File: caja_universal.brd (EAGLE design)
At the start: 100 x 80 mm, 34 parts, among them IC2 AD620N, IC3 TL084P, IC4 TL084P, IC5 LM317LD, IC6 LM318N

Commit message: Esquematico finalizado (v0), board en progreso
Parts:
- removed IC5: LM317LD, linear:SO08
- removed JP10, JP11, JP12: (no value), pinhead:1X01
- removed JP4, JP5, JP8, JP9: (no value), pinhead:1X02
- removed R12: (no value), resistor:0204/7
- added BNC-HALL, BNC-HR, BNC-PRESION, BNC-TENSION: (no value), pinhead:1X02
- added HALL-PLACA, HR-PLACA, TENSION-PLACA: (no value), pinhead:1X01
- added LM385-OFFSET: 2SC945, transistor:TO92-ECB
- added POT-GAIN, POT-OFFSET: (no value), pinhead:1X03
- added R-REG-FCORR: 10k, resistor:0204/7
- R-REG-OFFSET: value (none) -> 680k
- R10, R7, R8, R9: value (none) -> 10k
- R3, R4: value (none) -> 20k
- R5: value (none) -> 1k
- R6: value (none) -> 2k
- moved OPAMP-FCORR 110.8 mm to (30.5, 57.1), turned to 180 degrees
- moved PRESION-PLACA 105.2 mm to (77.5, 72.4)
- moved CHECK 103.8 mm to (55.9, 72.4)
- moved CORRIENTE-PLACA 95.6 mm to (40.6, 72.4), turned to 180 degrees
- moved RCHECK 85.2 mm to (57.1, 63.5), turned to 270 degrees
- moved ALIMENTACION-PLACA 80.7 mm to (17.8, 63.5)
- moved CHECK-LED 80.1 mm to (55.9, 54.6), turned to 180 degrees
- moved ALIMENTACION-BATERIAS 71.1 mm to (20.3, 74.9)
- moved LM385-FCORR 60.5 mm to (11.4, 50.8), turned to 270 degrees
- moved SWITCH 60.2 mm to (19.1, 68.6)
- renumbered IC2 to PREAMP-PRESION, IC6 to SEGUIDOS-PREAMP-PRESION, R2 to R-REG-OFFSET
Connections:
- new net -1.25V: IC3.8, IC3.9, POT-OFFSET.3
- new net 1.25V: IC3.1, IC3.2, POT-OFFSET.2, R3.1
- new net HALL: BNC-HALL.1, HALL-PLACA.1
- new net HR: BNC-HR.1, HR-PLACA.1
- new net N$10: IC3.13, R5.2, R6.1
- new net N$11: IC3.14, IC4.3, R6.2
- new net N$12: IC4.6, R10.2, R7.1, R9.2
- new net N$13: R9.1, SEGUIDOS-PREAMP-PRESION.2, SEGUIDOS-PREAMP-PRESION.6
- new net N$14: IC4.10, IC4.7, R7.2
- new net N$15: IC4.8, IC4.9, R8.1
- new net N$16: IC4.13, POT-GAIN.3, R8.2
- new net N$6: IC3.6, R3.2, R4.1
- new net N$7: IC3.3, LM385-OFFSET.C, R-REG-OFFSET.2
- new net N$8: IC3.10, IC3.7, R4.2
- new net N$9: IC4.1, IC4.2, R10.1
- new net OFFSET: IC3.12, POT-OFFSET.1
- new net PRESION: BNC-PRESION.1, IC4.14, POT-GAIN.2
- new net TENSION: BNC-TENSION.1, TENSION-PLACA.1
- net +12V: now also R-REG-FCORR.2, R-REG-OFFSET.1, SEGUIDOS-PREAMP-PRESION.7
- net -12V: now also SEGUIDOS-PREAMP-PRESION.4
- net 0V: now also BNC-HALL.2, BNC-HR.2, BNC-PRESION.2, BNC-TENSION.2, IC3.5, IC4.5, LM385-OFFSET.B, LM385-OFFSET.E, R5.1
- net N$3: now also R-REG-FCORR.1
- net PRESION-PREAMP: now also SEGUIDOS-PREAMP-PRESION.3
- net V+: no longer SEGUIDOS-PREAMP-PRESION.7
- net V-: no longer SEGUIDOS-PREAMP-PRESION.4
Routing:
- net +12V: track 0.00 -> 45.3 mm
- net -12V: track 0.00 -> 14.0 mm
- net N$3: track 0.00 -> 10.2 mm
- net -12VBAT: track 0.00 -> 6.35 mm
- net +12VBAT: track 0.00 -> 6.35 mm
- net N$2: track 0.00 -> 5.08 mm
- net N$1: track 0.00 -> 5.08 mm
- added copper zone on layer 1, net 0V

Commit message: Avanzando...
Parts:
- moved LM385-OFFSET 154.7 mm to (67.3, 40.6), turned to 270 degrees
- moved R3 122.1 mm to (66.0, 10.2)
- moved SEGUIDOS-PREAMP-PRESION 114.8 mm to (36.8, 34.3), turned to 180 degrees
- moved R4 102.4 mm to (76.2, 10.2)
- moved R6 99.2 mm to (58.4, 27.9), turned to 180 degrees
- moved R10 92.0 mm to (48.3, 22.9), turned to 180 degrees
- moved IC3 91.1 mm to (67.3, 19.1)
- moved R-REG-OFFSET 90.9 mm to (49.5, 34.3), turned to 90 degrees
- moved R5 88.4 mm to (58.4, 31.8)
- moved R7 88.4 mm to (35.6, 22.9), turned to 180 degrees
- moved IC4 88.1 mm to (44.5, 15.2), turned to 180 degrees
- moved RG-PRESION 78.9 mm to (27.9, 34.3), turned to 90 degrees
- moved R8 77.8 mm to (43.2, 6.35)
- moved R-FCORR 74.3 mm to (39.4, 71.1), turned to 180 degrees
- moved R9 69.9 mm to (35.6, 25.4)
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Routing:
- net +12V: track 45.3 -> 104.1 mm
- net -12V: track 14.0 -> 52.1 mm
- net PRESION: track 0.00 -> 35.6 mm
- net N$16: track 0.00 -> 25.4 mm
- net N$11: track 0.00 -> 24.1 mm
- net N$8: track 0.00 -> 22.9 mm
- net N$7: track 0.00 -> 20.3 mm
- net N$13: track 0.00 -> 19.1 mm
- net TENSION: track 0.00 -> 15.2 mm
- net N$12: track 0.00 -> 14.0 mm
- net HR: track 0.00 -> 14.0 mm
- net 1.25V: track 0.00 -> 14.0 mm
- net N$10: track 0.00 -> 8.89 mm
- net N$6: track 0.00 -> 7.62 mm
- net N$15: track 0.00 -> 7.62 mm
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
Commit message: Terminada primera version de la placa
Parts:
- removed ALIMENTACION-BATERIAS, ALIMENTACION-PLACA: (no value), pinhead:1X03
- removed CORRIENTE-PLACA, PRESION-PLACA: (no value), pinhead:1X02
- removed LM385-FCORR, LM385-OFFSET: 2SC945, transistor:TO92-ECB
- removed OPAMP-FCORR, SEGUIDOS-PREAMP-PRESION: LM318N, linear:DIL08
- removed PREAMP-PRESION: AD620N, analog-devices:DIL08
- removed R-FCORR, RG-PRESION: 820, resistor:0204/7
- removed R-REG-FCORR: 10k, resistor:0204/7
- removed R-REG-OFFSET: 680k, resistor:0204/7
- removed SWITCH: (no value), pinhead:1X04
- removed TENSION-PLACA: (no value), pinhead:1X01
- added +12V-FUSE, -12V-FUSE, I-PLACA, P-PLACA, T-PLACA: (no value), pinhead:1X02
- added D1, D2: LM385, lm385:TO-92
- added IC1, IC5: NE5534AN, linear:DIL08
- added IC2: AD620N, analog-devices:DIL08
- added R1, R2: 820, resistor:0204/7
- added R11: 10k, resistor:0204/7
- added R12: 680k, resistor:0204/7
- added SWITCH-GRAL, SWITCH-P: (no value), pinhead:1X04
- added V-BAT, V-PLACA: (no value), pinhead:1X03
- BNC-HALL, BNC-HR, BNC-PRESION, BNC-TENSION: value (none) -> A1944-50; device pinhead:1X02 -> con-coax:A1944
- HALL-PLACA, HR-PLACA: device pinhead:1X01 -> pinhead:1X02
- moved BNC-TENSION 69.5 mm to (36.2, 7.79), turned to 0 degrees
- moved POT-OFFSET 65.4 mm to (4.73, 35.0), turned to 270 degrees
- moved BNC-HALL 55.1 mm to (94.5, 7.79), turned to 0 degrees
- moved BNC-HR 52.4 mm to (63.8, 8.00), turned to 0 degrees
- moved BNC-PRESION 45.9 mm to (7.53, 7.49)
- moved R4 37.7 mm to (50.7, 37.9), turned to 180 degrees
- moved POT-GAIN 30.6 mm to (4.77, 25.1), turned to 90 degrees
- moved R10 27.0 mm to (23.7, 33.9)
- moved HALL-PLACA 25.7 mm to (56.4, 60.6)
- moved HR-PLACA 25.2 mm to (67.1, 60.5), turned to 180 degrees
- moved R3 24.7 mm to (58.4, 33.6), turned to 180 degrees
- moved R8 22.8 mm to (23.2, 17.3)
- moved IC4 22.7 mm to (23.9, 24.8)
- moved R9 22.6 mm to (20.0, 41.9)
- moved R7 21.9 mm to (19.6, 37.9)
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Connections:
- net PRESION renamed POUT
- removed net 0VBAT: ALIMENTACION-BATERIAS.2
- removed net PRESION-PREAMP: PREAMP-PRESION.6, SEGUIDOS-PREAMP-PRESION.3
- new net +12V-PRESION: CHECK.1, IC1.7, IC2.7, IC5.7, R11.2, R12.1, SWITCH-P.2
- new net +12VFUSE: +12V-FUSE.1, SWITCH-GRAL.1
- new net -12V-PRESION: IC1.4, IC2.4, IC5.4, SWITCH-P.4
- new net -12VFUSE: -12V-FUSE.1, SWITCH-GRAL.3
- new net P-PREAMP: IC2.6, IC5.3
- net +12V: now also +12V-FUSE.2, SWITCH-P.1, V-PLACA.1; no longer ALIMENTACION-PLACA.1, CHECK.1, OPAMP-FCORR.7, PREAMP-PRESION.7, R-REG-FCORR.2, R-REG-OFFSET.1, SEGUIDOS-PREAMP-PRESION.7, SWITCH.1
- net +12VBAT: now also SWITCH-GRAL.2, V-BAT.1; no longer ALIMENTACION-BATERIAS.1, SWITCH.2
- net +I: now also I-PLACA.1, IC1.6; no longer CORRIENTE-PLACA.1, OPAMP-FCORR.6
- net -12V: now also -12V-FUSE.2, SWITCH-P.3, V-PLACA.3; no longer ALIMENTACION-PLACA.3, OPAMP-FCORR.4, PREAMP-PRESION.4, SEGUIDOS-PREAMP-PRESION.4, SWITCH.3
- net -12VBAT: now also SWITCH-GRAL.4, V-BAT.3; no longer ALIMENTACION-BATERIAS.3, SWITCH.4
- net -I: now also I-PLACA.2, IC1.2, R2.2; no longer CORRIENTE-PLACA.2, OPAMP-FCORR.2, R-FCORR.2
- net 0V: now also BNC-HALL.3, BNC-HALL.4, BNC-HALL.5, BNC-HR.3, BNC-HR.4, BNC-HR.5, BNC-PRESION.3, BNC-PRESION.4, BNC-PRESION.5, BNC-TENSION.3, BNC-TENSION.4, BNC-TENSION.5, D1.-, D1.FB, D2.-, D2.FB, IC2.5, R2.1, V-BAT.2, V-PLACA.2; no longer ALIMENTACION-PLACA.2, LM385-FCORR.B, LM385-FCORR.E, LM385-OFFSET.B, LM385-OFFSET.E, PREAMP-PRESION.5, R-FCORR.1
- net HALL: now also HALL-PLACA.2; no longer HALL-PLACA.1
- net HR: now also HR-PLACA.2; no longer HR-PLACA.1
- net N$13: now also IC5.2, IC5.6; no longer SEGUIDOS-PREAMP-PRESION.2, SEGUIDOS-PREAMP-PRESION.6
- net N$3: now also D2.+, IC1.3, R11.1; no longer LM385-FCORR.C, OPAMP-FCORR.3, R-REG-FCORR.1
- net N$4: now also IC2.1, R1.2; no longer PREAMP-PRESION.1, RG-PRESION.2
- net N$5: now also IC2.8, R1.1; no longer PREAMP-PRESION.8, RG-PRESION.1
- net N$7: now also D1.+, R12.2; no longer LM385-OFFSET.C, R-REG-OFFSET.2
- net P+: now also IC2.3, P-PLACA.1; no longer PREAMP-PRESION.3, PRESION-PLACA.1
- net P-: now also IC2.2, P-PLACA.2; no longer PREAMP-PRESION.2, PRESION-PLACA.2
- net TENSION: now also T-PLACA.2; no longer TENSION-PLACA.1
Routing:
- net +12V-PRESION: track 0.00 -> 163.9 mm
- net V-: track 0.00 -> 146.7 mm
- net N$7: track 20.3 -> 134.4 mm
- net +12V: track 104.1 -> 203.0 mm
- net OFFSET: track 0.00 -> 89.6 mm
- net TENSION: track 15.2 -> 104.8 mm
- net HALL: track 6.35 -> 85.6 mm
- net HR: track 14.0 -> 85.0 mm
- net -12V: track 52.1 -> 119.9 mm
- net 1.25V: track 14.0 -> 81.7 mm
- net -1.25V: track 0.00 -> 62.8 mm
- net -12V-PRESION: track 0.00 -> 61.4 mm
- net V+: track 0.00 -> 55.4 mm
- net +I: track 0.00 -> 31.9 mm
- net P-PREAMP: track 0.00 -> 26.8 mm
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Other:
- board size 100 x 80 mm -> 117.8 x 66.5 mm

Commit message: Version para revisar (JyG)
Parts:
- IC1, IC5: value NE5534AN -> AD711N; device linear:DIL08 -> analog-devices:DIL08
- moved V-PLACA 50.2 mm to (61.0, 80.9)
- moved HALL-PLACA 42.9 mm to (94.4, 80.6)
- moved -12V-FUSE 32.4 mm to (83.8, 67.9), turned to 90 degrees
- moved D1 28.2 mm to (65.7, 44.4), turned to 270 degrees
- moved HR-PLACA 26.2 mm to (84.1, 80.5)
- moved +12V-FUSE 25.0 mm to (79.2, 67.7), turned to 90 degrees
- moved I-PLACA 21.9 mm to (31.6, 80.7)
- moved SWITCH-P 21.5 mm to (19.8, 80.7)
- moved D2 20.6 mm to (57.7, 56.3), turned to 180 degrees
- moved CHECK 20.6 mm to (44.0, 80.6)
- moved P-PLACA 20.1 mm to (2.33, 80.4)
- moved T-PLACA 20.1 mm to (73.0, 80.6)
- moved IC1 19.6 mm to (59.0, 67.0)
- moved RCHECK 18.8 mm to (70.8, 68.0)
- moved POT-GAIN 17.4 mm to (0.23, 41.9), turned to 270 degrees
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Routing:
- net +12V: track 203.0 -> 65.3 mm
- net V-: track 146.7 -> 34.8 mm
- net N$7: track 134.4 -> 35.3 mm
- net +12V-PRESION: track 163.9 -> 116.3 mm, vias 0 -> 1
- net -12V: track 119.9 -> 82.3 mm
- net POUT: track 50.0 -> 81.6 mm
- net -I: track 19.2 -> 43.8 mm
- net N$13: track 37.1 -> 17.3 mm
- net V+: track 55.4 -> 36.1 mm
- net +12VBAT: track 26.4 -> 9.82 mm
- net -12VBAT: track 24.4 -> 9.94 mm
- net -12V-PRESION: track 61.4 -> 75.6 mm
- net N$16: track 33.1 -> 47.2 mm
- net N$2: track 15.4 -> 29.1 mm
- net OFFSET: track 89.6 -> 76.9 mm
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- added copper zone on layer 16, net 0V
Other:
- board size 117.8 x 66.5 mm -> 137.8 x 101.5 mm
- board text added: "LSD - Tecnologia Hibrida de Cajas"

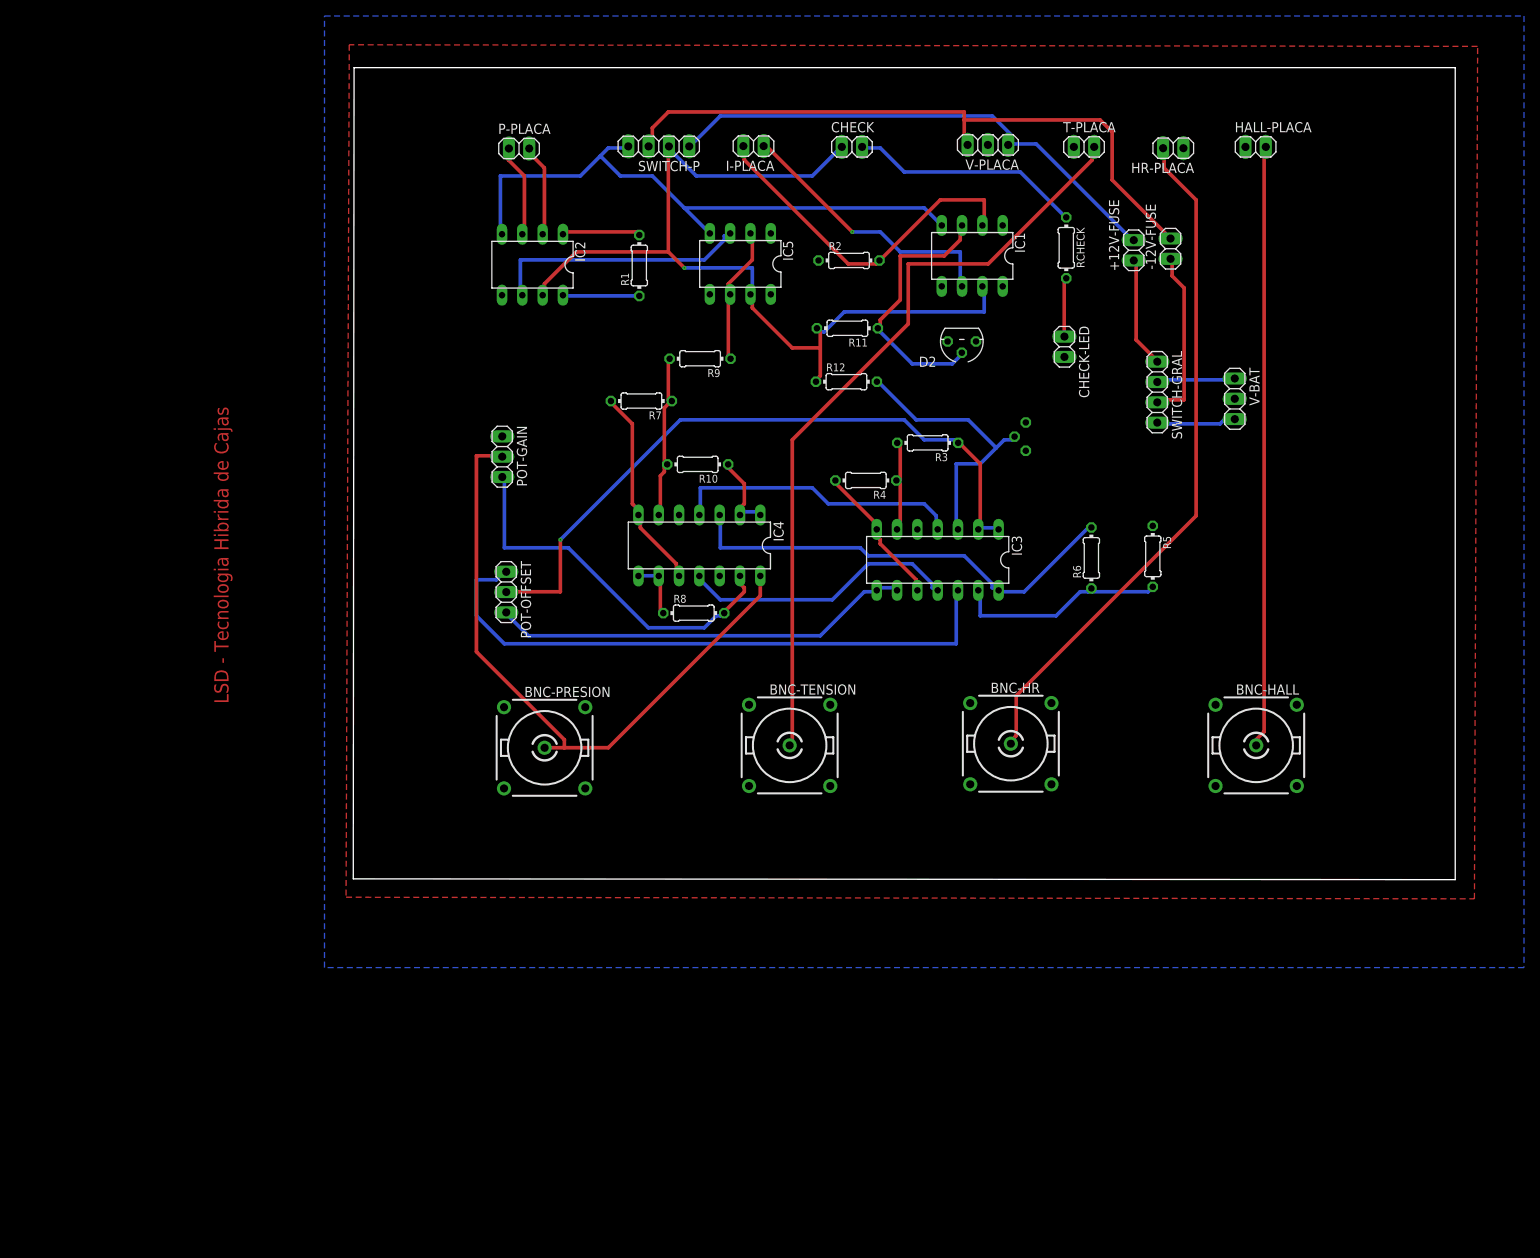
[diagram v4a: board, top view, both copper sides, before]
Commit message: Agregamos con Juan uno GND que faltaban. Falta ver alimentacion de TL084 y cambiar valor resistencia del LED
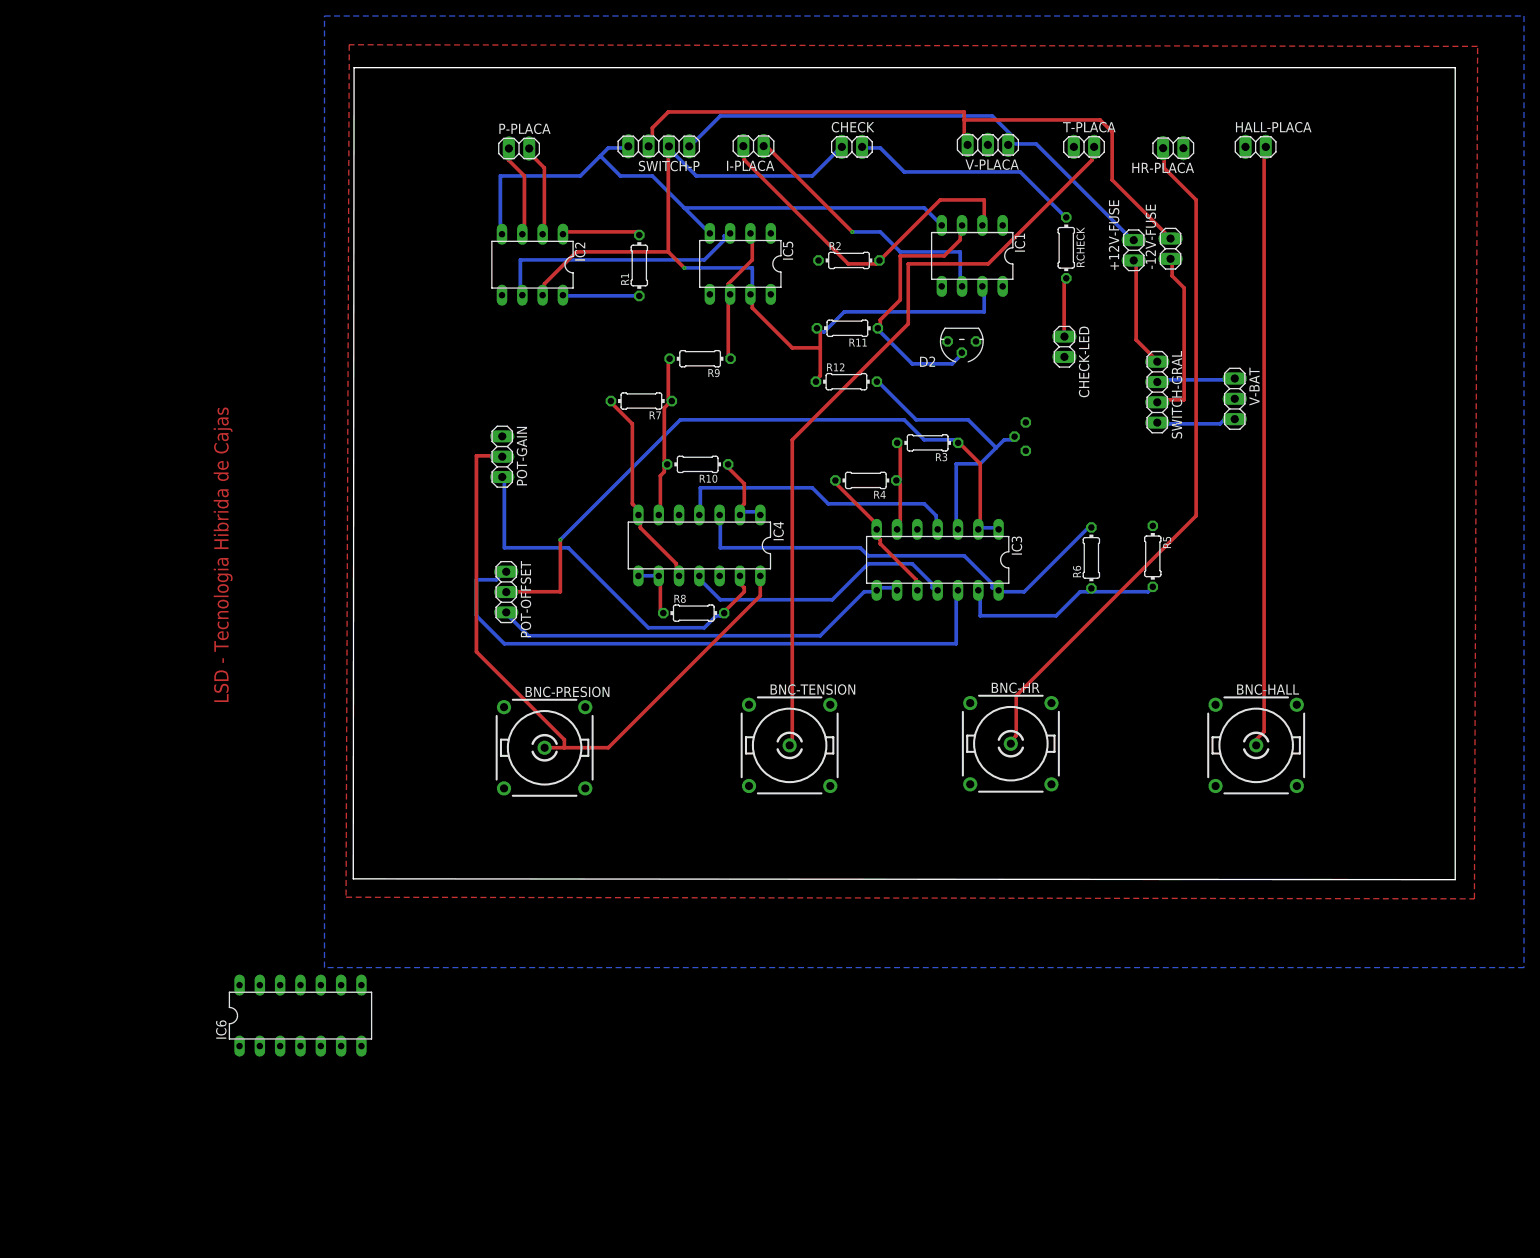
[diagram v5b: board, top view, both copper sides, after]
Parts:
- added IC6: TL084P, linear:DIL14
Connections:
- net 0V: now also IC4.12, POT-GAIN.1
- net V+: now also IC6.4
- net V-: now also IC6.11
